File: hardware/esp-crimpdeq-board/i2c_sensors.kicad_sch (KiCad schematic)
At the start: 14 parts, among them U1 SHTC3, U2 ICM-42670-P, U7 MAX17262

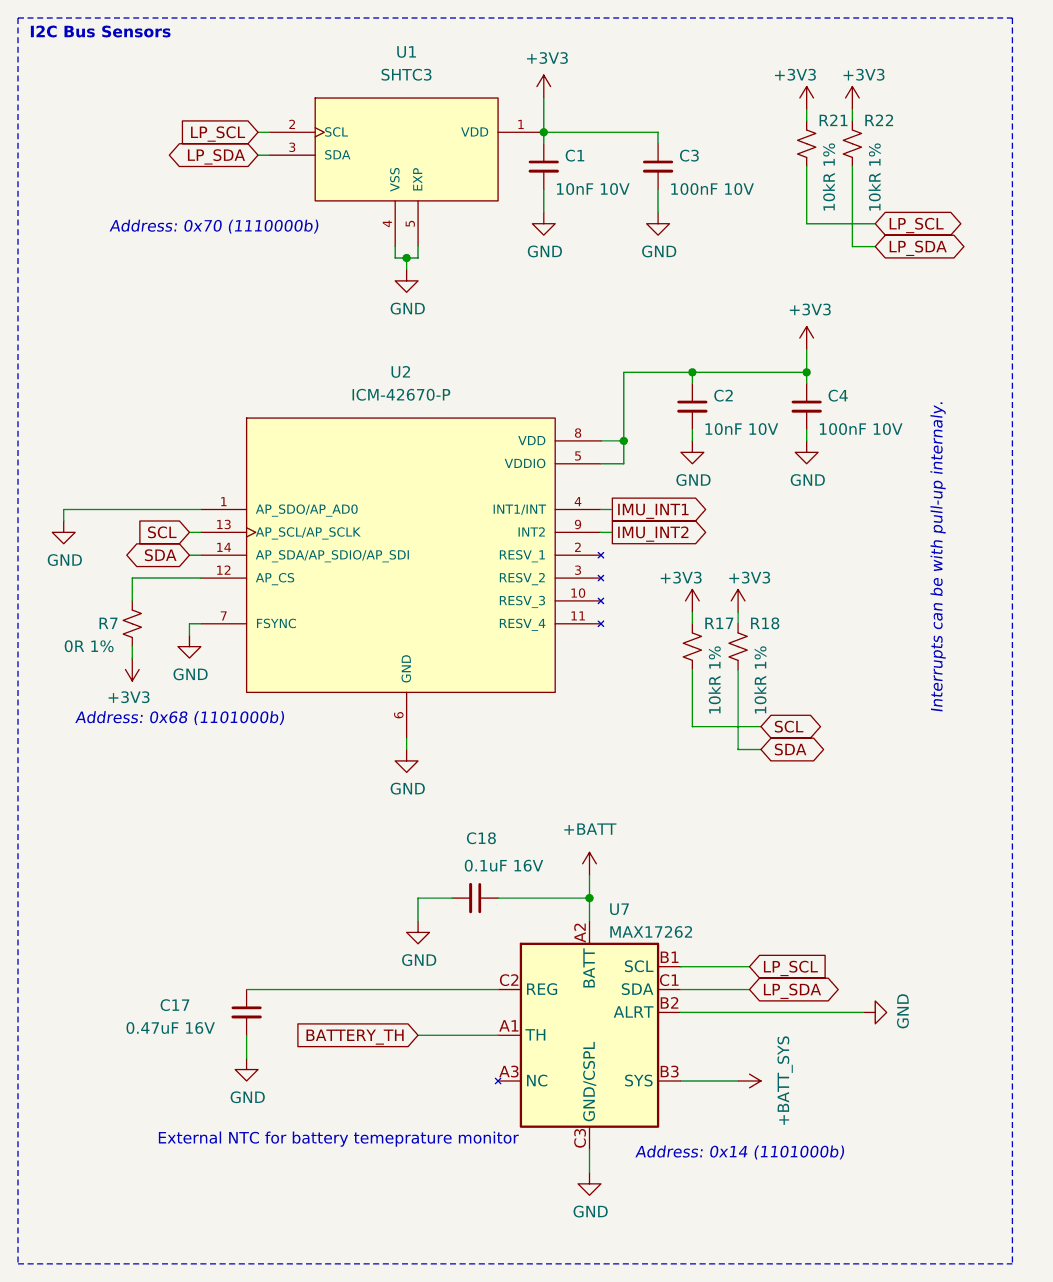
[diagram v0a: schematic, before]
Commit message: Ordering sdchematic in different sheets
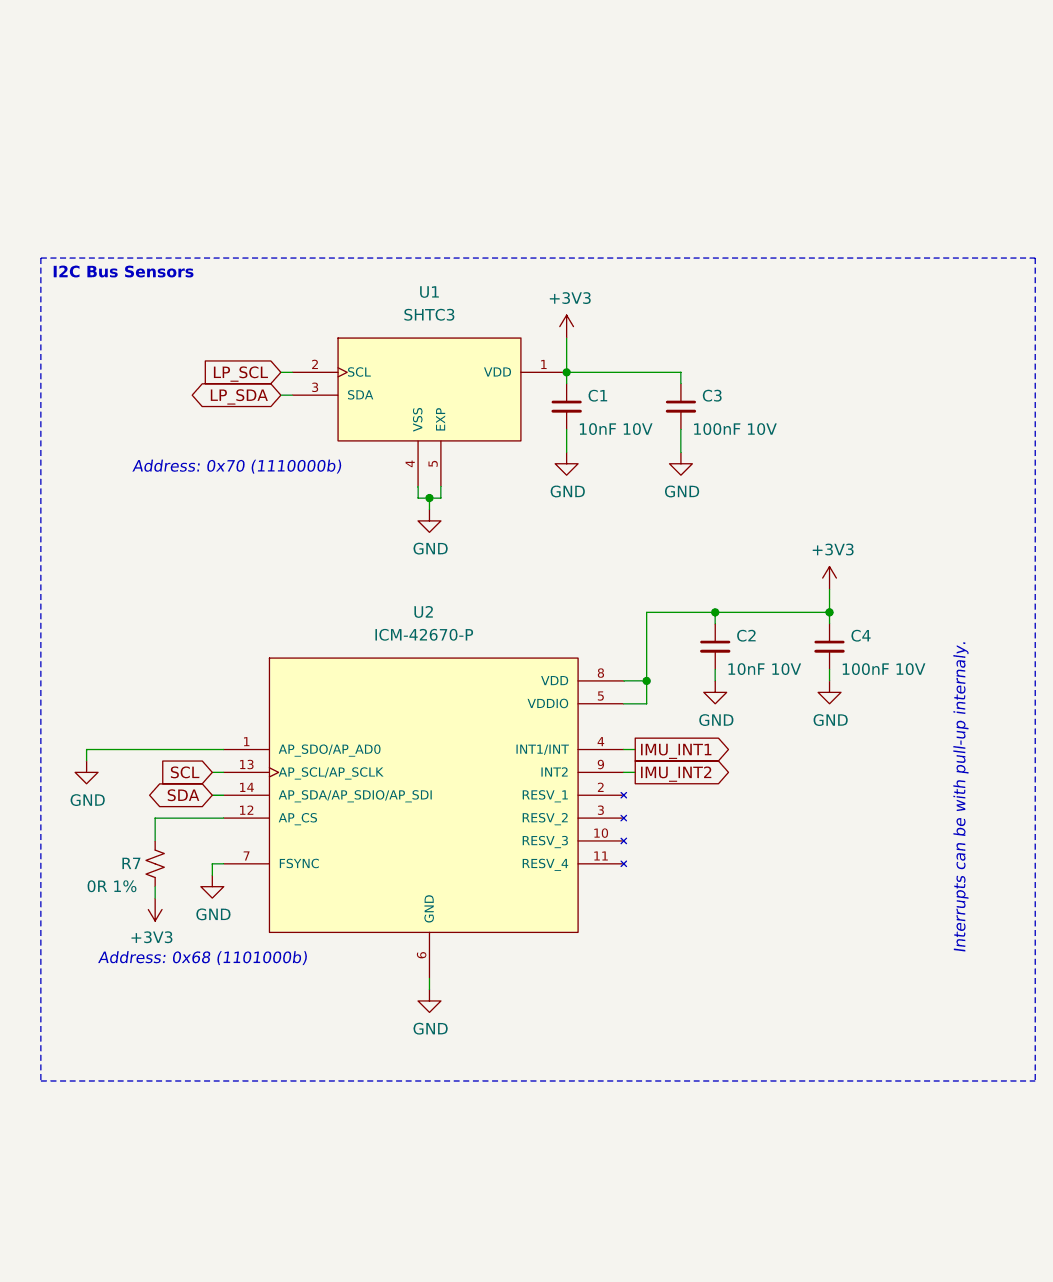
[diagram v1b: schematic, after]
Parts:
- removed C17: 0.47uF 16V, Capacitor_SMD:C_0603_1608Metric, symbol Device:C_Small
- removed C18: 0.1uF 16V, Capacitor_SMD:C_0603_1608Metric, symbol Device:C_Small
- removed R17, R18, R21, R22: 10kR 1%, Resistor_SMD:R_0402_1005Metric, symbol Device:R_Small_US
- removed U7: MAX17262, Package_BGA:WLP-9_1.468x1.448mm_Layout3x3_P0.4mm, symbol PCM_Maxim:MAX17262
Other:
- note removed: "Address: 0x14 (1101000b)"
- note removed: "External NTC for battery temeprature monitor"
- moved on the sheet: C1, C2, C3, C4, R7, U1, U2

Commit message: Cleaned schematic
- Pending connectors
- Pending BOM and footprints review
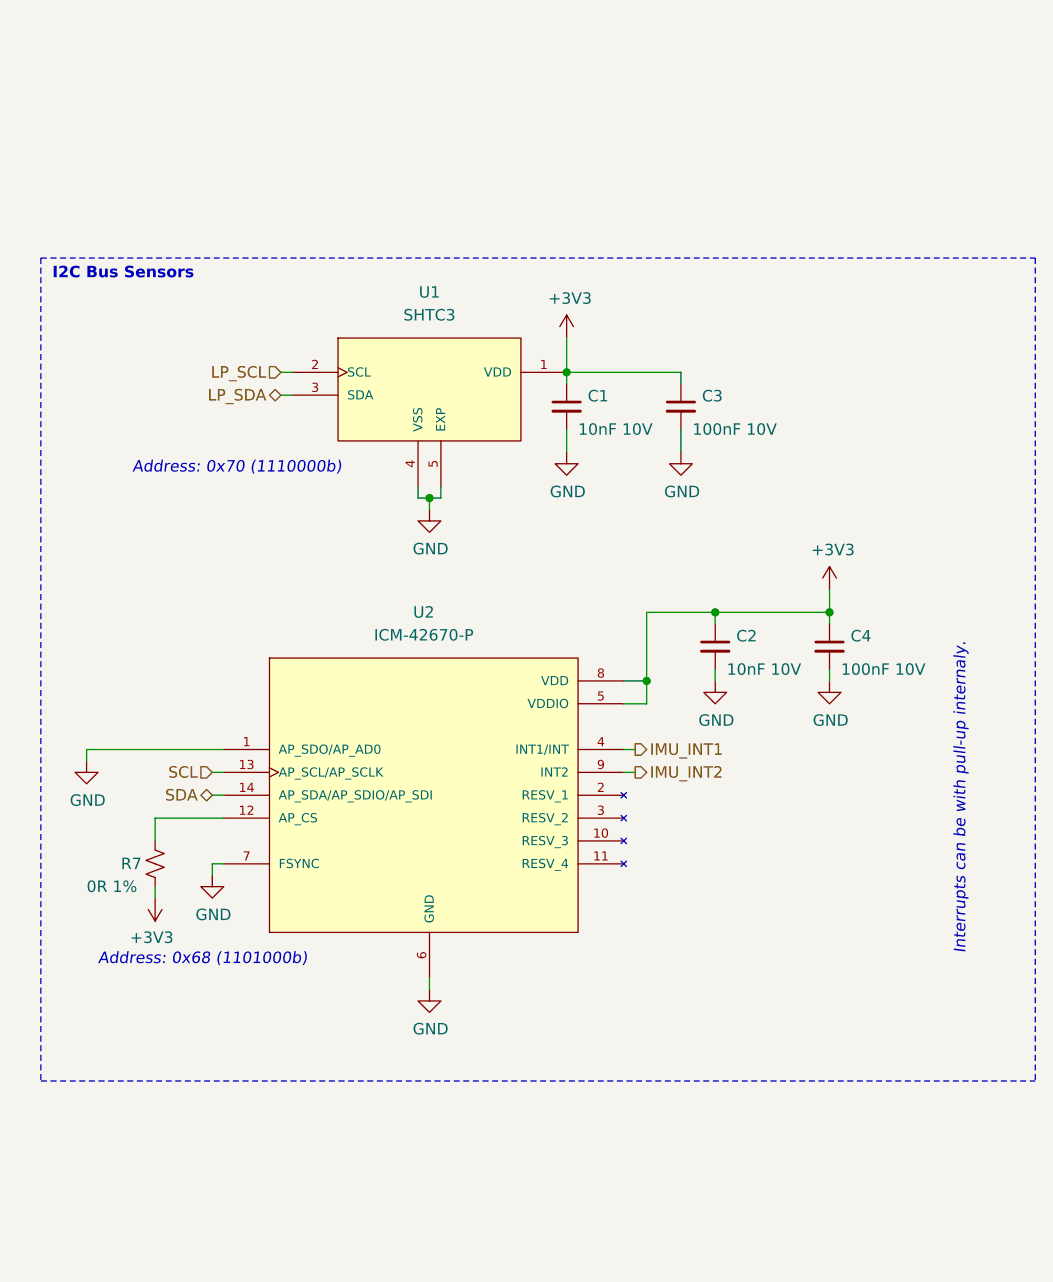
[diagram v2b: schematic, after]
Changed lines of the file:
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@@
 		)
 	)
-	(global_label "LP_SCL"
-		(shape input)
-		(at 115.57 59.69 180)
-		(fields_autoplaced yes)
+	(hierarchical_label "LP_SDA"
+		(shape bidirectional)
+		(at 115.57 62.23 180)
 		(effects
 			(font
@@
 			(justify right)
 		)
-		(property "Intersheetrefs" "${INTERSHEET_REFS}"
-			(at 106.4657 59.69 0)
-			(effects
-				(font
-					(size 1.27 1.27)
-				)
-				(justify right)
-				(hide yes)
-			)
-		)
 	)
-	(global_label "SCL"
+	(hierarchical_label "SCL"
 		(shape input)
 		(at 107.95 104.14 180)
-		(fields_autoplaced yes)
 		(effects
 			(font
@@
 			(justify right)
 		)
-		(property "Intersheetrefs" "${INTERSHEET_REFS}"
-			(at 102.1114 104.14 0)
-			(effects
-				(font
-					(size 1.27 1.27)
-				)
-				(justify right)
-				(hide yes)
-			)
-		)
 	)
-	(global_label "IMU_INT2"
+	(hierarchical_label "IMU_INT2"
 		(shape output)
 		(at 154.94 104.14 0)
-		(fields_autoplaced yes)
 		(effects
 			(font
@@
 			(justify left)
 		)
-		(property "Intersheetrefs" "${INTERSHEET_REFS}"
-			(at 165.7377 104.14 0)
-			(effects
-				(font
-					(size 1.27 1.27)
-				)
-				(justify left)
-				(hide yes)
+	)
+	(hierarchical_label "SDA"
+		(shape bidirectional)
+		(at 107.95 106.68 180)
+		(effects
+			(font
+				(size 1.27 1.27)
 			)
+			(justify right)
 		)
 	)
-	(global_label "IMU_INT1"
+	(hierarchical_label "IMU_INT1"
 		(shape output)
 		(at 154.94 101.6 0)
-		(fields_autoplaced yes)
 		(effects
 			(font
@@
 			(justify left)
 		)
-		(property "Intersheetrefs" "${INTERSHEET_REFS}"
-			(at 165.7377 101.6 0)
-			(effects
-				(font
-					(size 1.27 1.27)
-				)
-				(justify left)
-				(hide yes)
-			)
-		)
 	)
-	(global_label "SDA"
-		(shape bidirectional)
-		(at 107.95 106.68 180)
-		(fields_autoplaced yes)
+	(hierarchical_label "LP_SCL"
+		(shape input)
+		(at 115.57 59.69 180)
 		(effects
 			(font
@@
 			(justify right)
 		)
-		(property "Intersheetrefs" "${INTERSHEET_REFS}"
-			(at 101.0984 106.68 0)
-			(effects
-				(font
-					(size 1.27 1.27)
-				)
-				(justify right)
-				(hide yes)
-			)
-		)
 	)
-	(global_label "LP_SDA"
-		(shape bidirectional)
-		(at 115.57 62.23 180)
-		(fields_autoplaced yes)
-		(effects
-			(font
-				(size 1.27 1.27)
-			)
-			(justify right)
-		)
-		(property "Intersheetrefs" "${INTERSHEET_REFS}"
-			(at 105.4527 62.23 0)
-			(effects
-				(font
-					(size 1.27 1.27)
-				)
-				(justify right)
-				(hide yes)
-			)
-		)
-	)
